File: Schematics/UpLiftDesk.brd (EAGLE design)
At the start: 37 parts

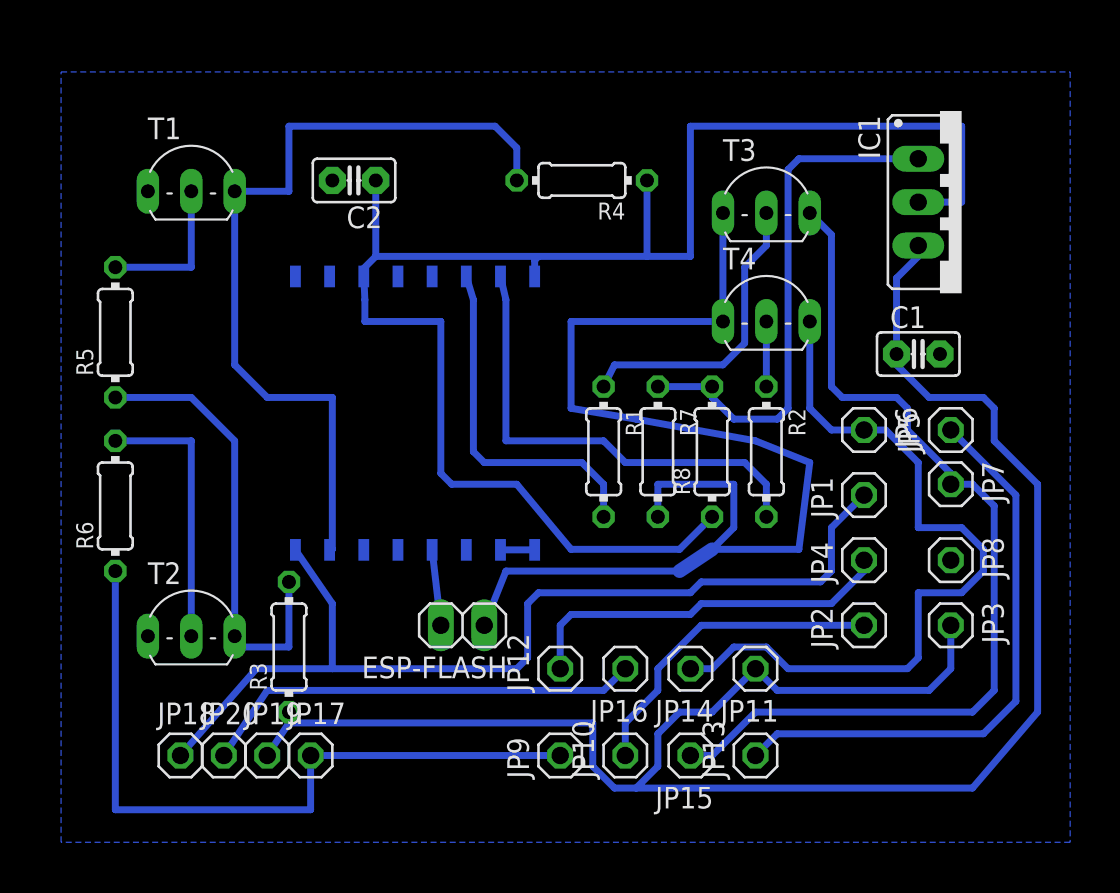
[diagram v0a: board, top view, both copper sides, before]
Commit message: Change ESP to through hole
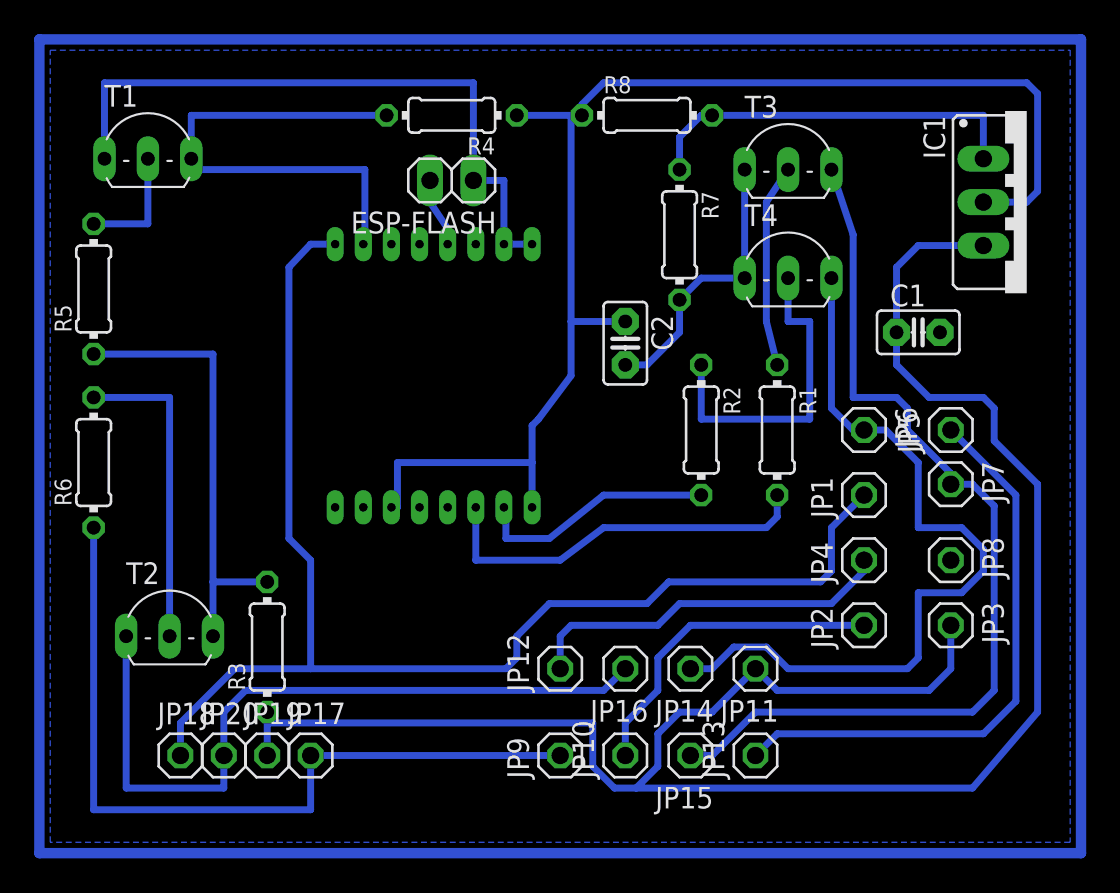
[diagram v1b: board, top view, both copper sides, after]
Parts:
- removed U$1: ESP-12, ESP8266:ESP-12
- added U$2: ESP-12-THROUGH, ESP8266:ESP-12-THROUGH
- moved ESP-FLASH 26.0 mm to (49.5, 40.0)
- moved R8 20.1 mm to (61.0, 43.8), turned to 0 degrees
- moved C2 18.5 mm to (59.7, 30.5), turned to 270 degrees
- moved R7 12.8 mm to (62.9, 36.8)
- moved R1 10.2 mm to (68.6, 25.4)
- moved R4 8.52 mm to (49.5, 43.8)
- moved R2 4.02 mm to (64.1, 25.4)
- moved IC1 3.81 mm to (83.2, 38.7)
- moved T1 3.18 mm to (31.8, 42.5)
- moved T3 2.84 mm to (69.2, 41.9)
- moved T4 2.84 mm to (69.2, 35.6)
- moved R5 2.84 mm to (28.6, 33.7)
- moved R6 2.84 mm to (28.6, 23.5)
- moved R3 1.27 mm to (38.7, 12.7)
- moved C1 1.27 mm to (76.8, 31.1)
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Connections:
- net 3.3V: now also U$2.CH_PD, U$2.VCC; no longer U$1.CH_PD, U$1.VCC
- net ESP-GPIO0: now also U$2.GPIO0; no longer U$1.GPIO0
- net ESP-GPIO12: now also U$2.GPIO12; no longer U$1.GPIO12
- net ESP-GPIO13: now also U$2.GPIO13; no longer U$1.GPIO13
- net ESP-RX: now also U$2.RX; no longer U$1.RX
- net ESP-TX: now also U$2.TX; no longer U$1.TX
- net GND: now also U$2.GND, U$2.GPIO15; no longer U$1.GND, U$1.GPIO15
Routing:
- net N$4: track 0.00 -> 217.2 mm
- net ESP-TX: track 57.5 -> 77.0 mm
- net ESP-RX: track 48.5 -> 29.2 mm
- net 3.3V: track 95.2 -> 78.8 mm
- net N$5: track 3.81 -> 19.0 mm
- net ESP-GPIO13: track 27.9 -> 14.3 mm
- net N$8: track 30.9 -> 22.8 mm
- net N$3: track 17.7 -> 11.9 mm
- net 5V: track 111.0 -> 115.7 mm
- net TX: track 43.2 -> 47.0 mm
- net N$2: track 15.9 -> 18.4 mm
- net ESP-GPIO12: track 20.6 -> 22.9 mm
- net N$6: track 8.89 -> 6.98 mm
- net UL-DOWN: track 54.4 -> 55.7 mm
- net UL-UP: track 45.0 -> 46.2 mm
